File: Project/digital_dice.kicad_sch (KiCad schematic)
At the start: 26 parts, among them SW1 SW_Push, U1 74LS04, U2 74LS93, U3 74LS08, U4 74LS32

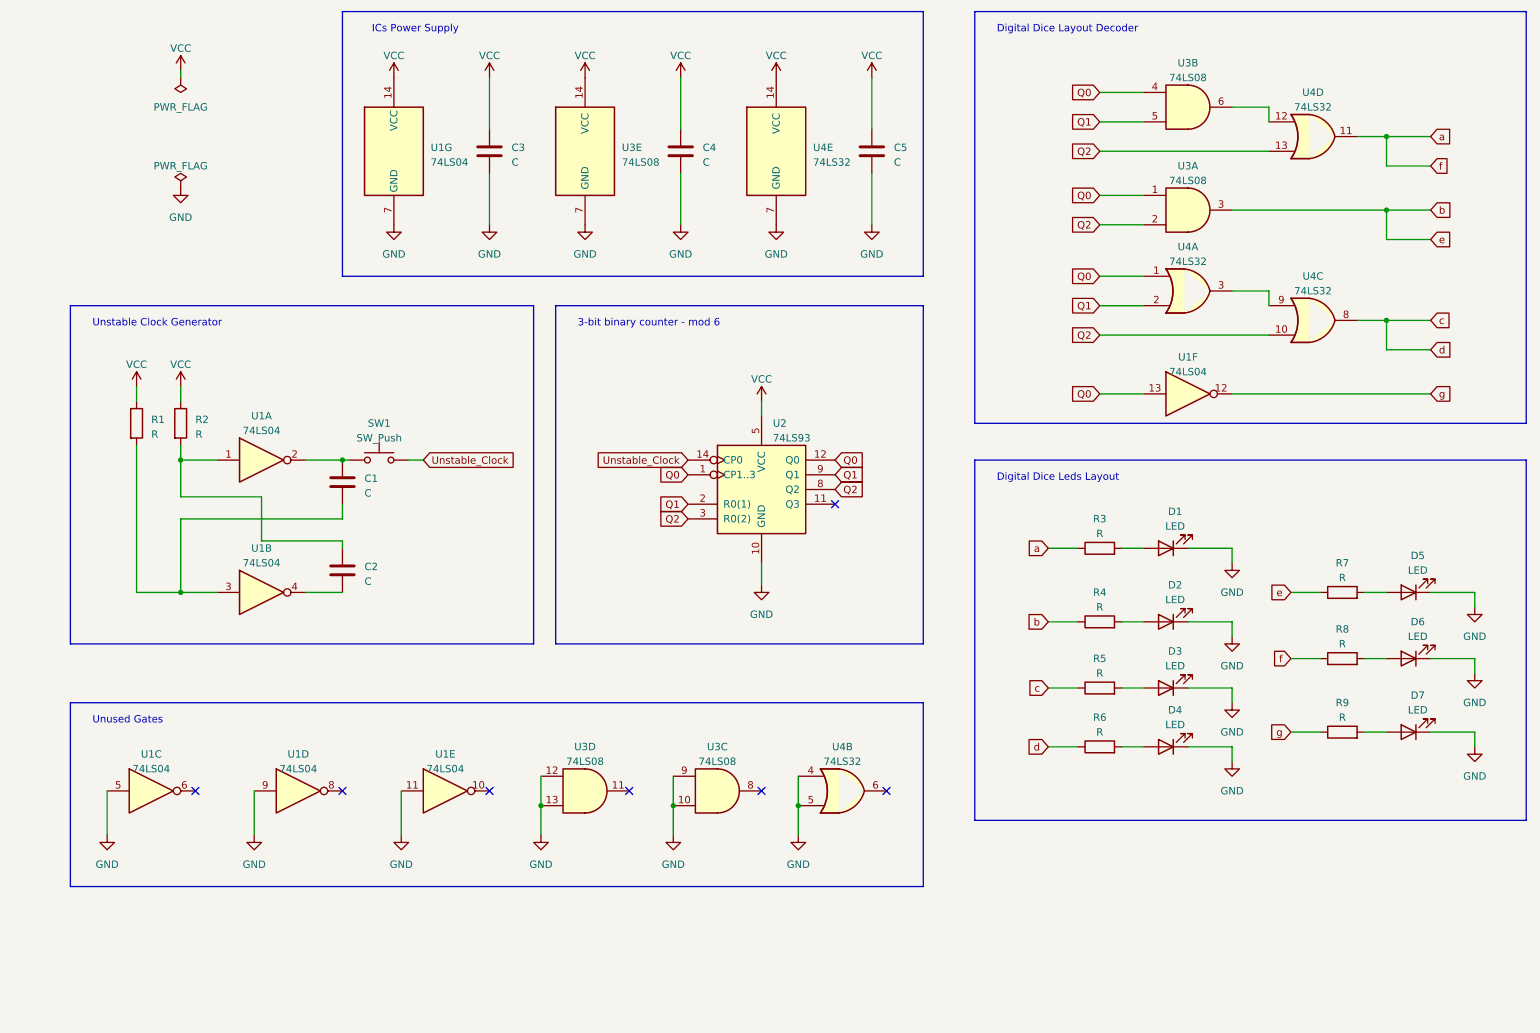
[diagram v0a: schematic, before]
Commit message: assigned components values and footprints
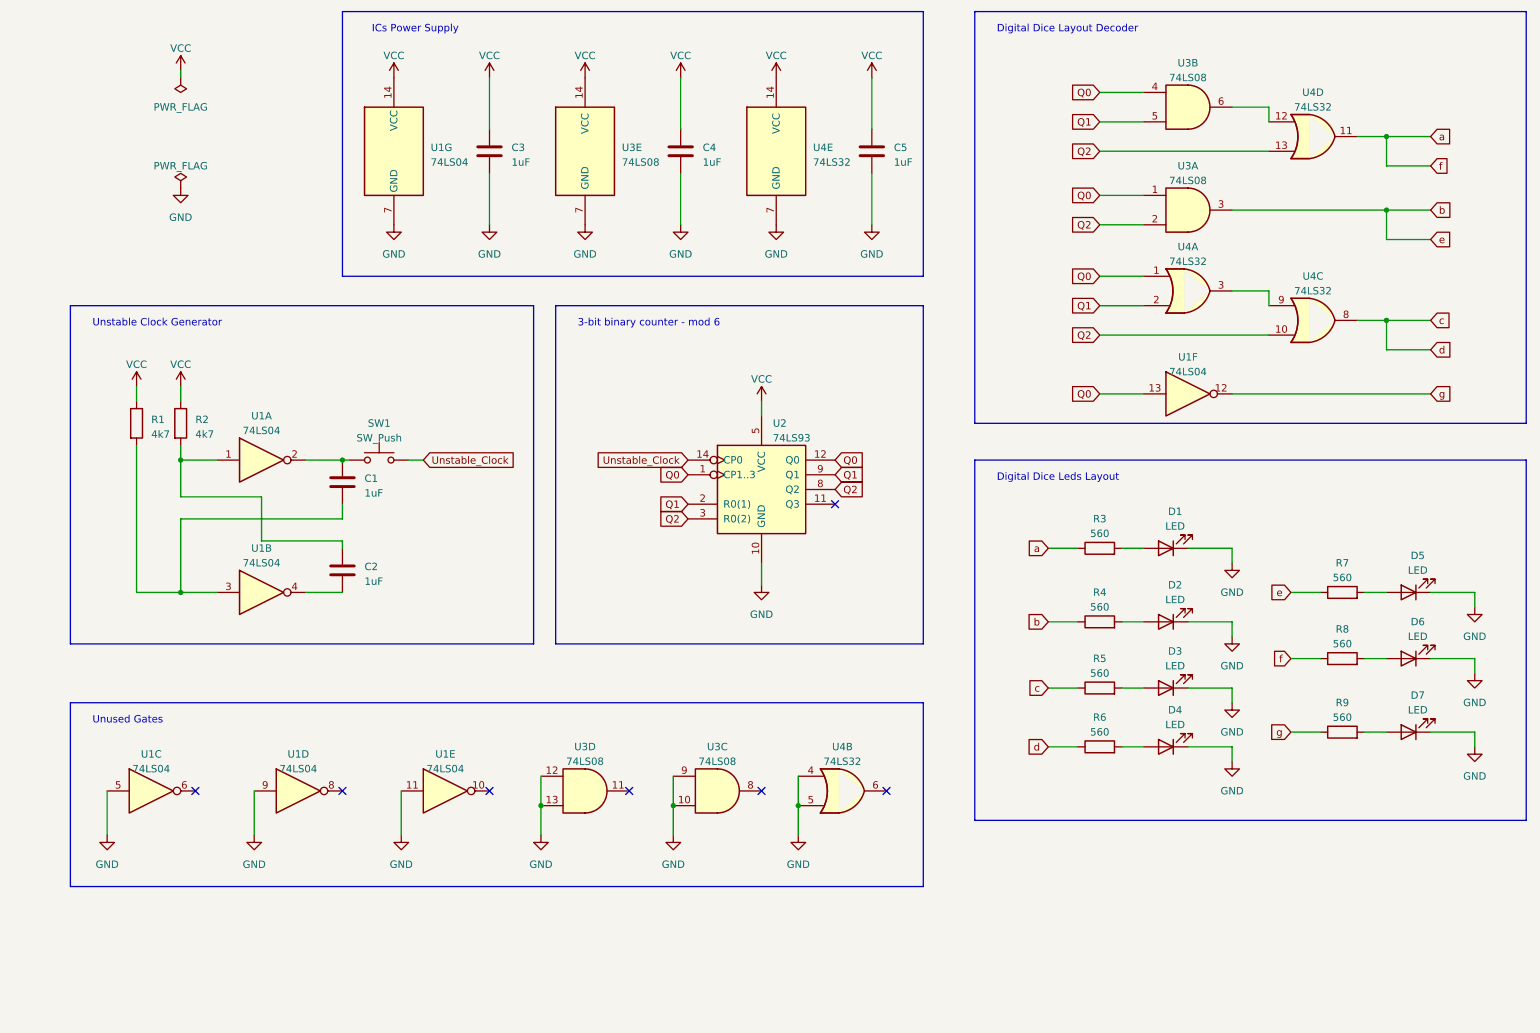
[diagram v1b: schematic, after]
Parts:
- C1, C2, C3, C4, C5: value C -> 1uF; footprint (none) -> Capacitor_THT:CP_Radial_D5.0mm_P2.50mm
- D1, D2, D3, D4, D5, D6, D7: footprint (none) -> LED_THT:LED_D5.0mm
- R1, R2: value R -> 4k7; footprint (none) -> Resistor_THT:R_Axial_DIN0207_L6.3mm_D2.5mm_P7.62mm_Horizontal
- R3, R4, R5, R6, R7, R8, R9: value R -> 560; footprint (none) -> Resistor_THT:R_Axial_DIN0207_L6.3mm_D2.5mm_P7.62mm_Horizontal
- SW1: footprint (none) -> Button_Switch_THT:SW_PUSH_6mm
- U1, U2, U3, U4: footprint (none) -> Package_DIP:DIP-14_W7.62mm

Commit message: changed leds and button to pin headers, added main power supply
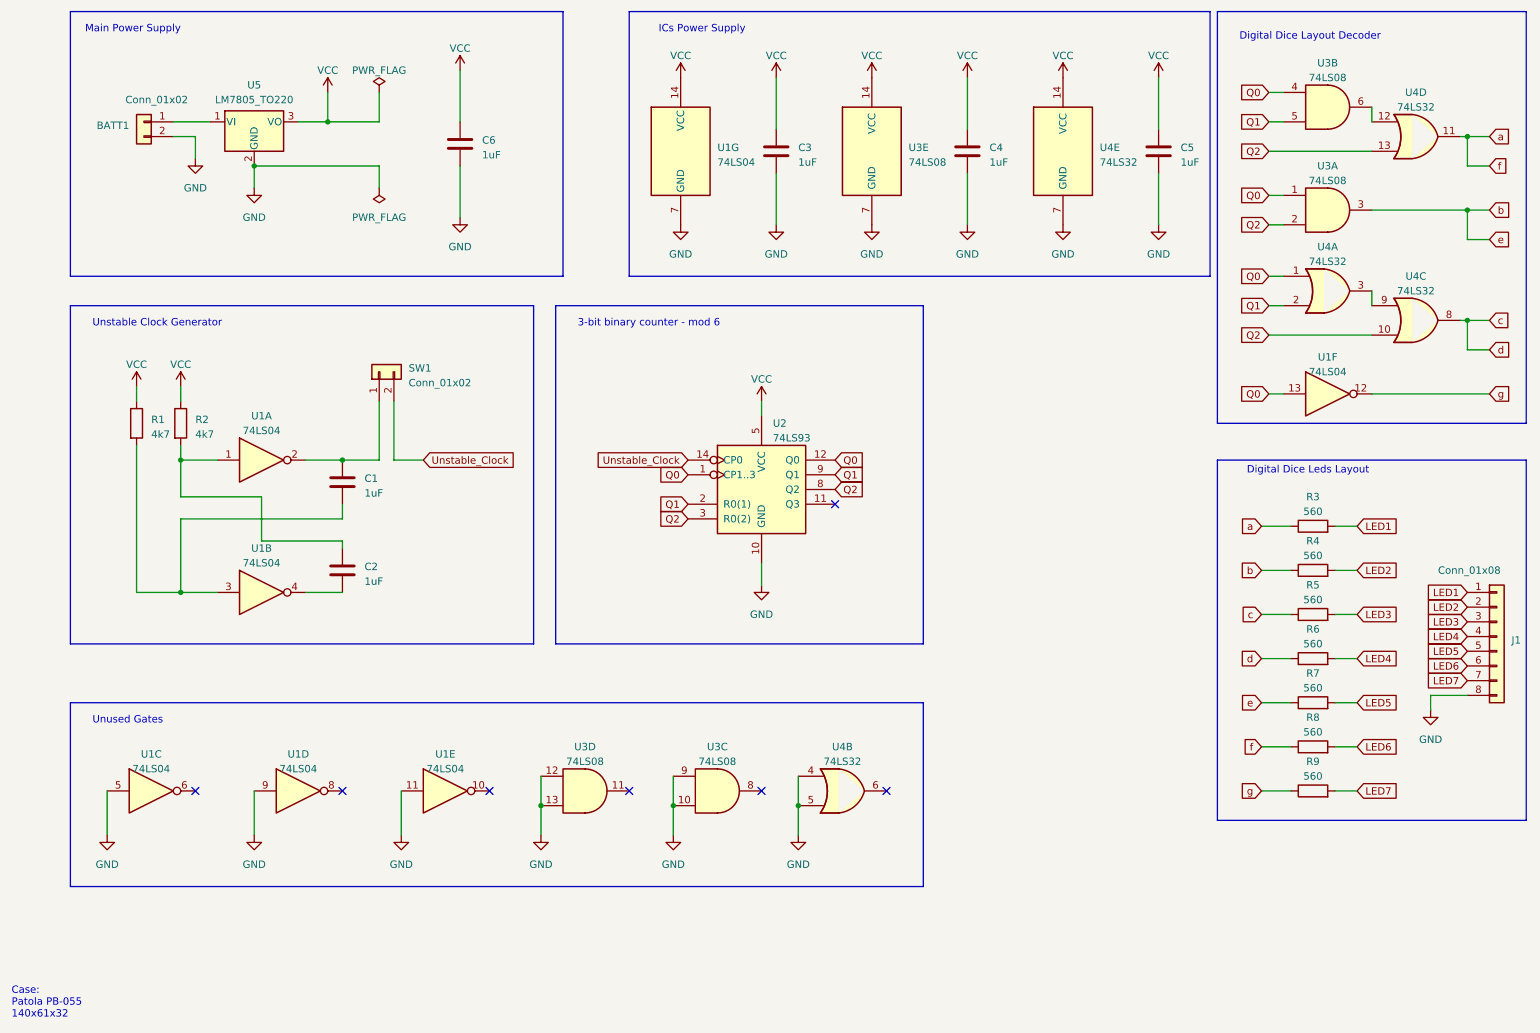
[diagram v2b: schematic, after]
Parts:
- removed D1, D2, D3, D4, D5, D6, D7: LED, LED_THT:LED_D5.0mm, symbol Device:LED
- removed SW1: SW_Push, Button_Switch_THT:SW_PUSH_6mm, symbol Switch:SW_Push
- added BATT1, SW1: Conn_01x02, Connector_PinHeader_2.54mm:PinHeader_1x02_P2.54mm_Vertical, symbol Connector_Generic:Conn_01x02
- added C6: 1uF, Capacitor_THT:CP_Radial_D5.0mm_P2.50mm, symbol Device:C
- added J1: Conn_01x08, Connector_PinHeader_2.54mm:PinHeader_1x08_P2.54mm_Vertical, symbol Connector_Generic:Conn_01x08
- added U5: LM7805_TO220, Package_TO_SOT_THT:TO-220-3_Vertical, symbol Regulator_Linear:LM7805_TO220
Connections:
- net GND: now also BATT1.2 (Pin_2), C6.2, J1.8 (Pin_8), U5.2 (GND)
- net Unstable_Clock: now also SW1.2 (Pin_2)
- net VCC: now also C6.1, U5.3 (VO)
- net LED3: now reaches R5.2
- net LED3: now also J1.3 (Pin_3)
- net LED2: now reaches R4.2
- net LED2: now also J1.2 (Pin_2)
- net LED6: now reaches R8.2
- net LED6: now also J1.6 (Pin_6)
- net LED1: now reaches R3.2
- net LED1: now also J1.1 (Pin_1)
- net at C1.1, U1.2: now also SW1.1 (Pin_1)
- net LED7: now reaches R9.2
- net LED7: now also J1.7 (Pin_7)
- net LED4: now reaches R6.2
- net LED4: now also J1.4 (Pin_4)
- net LED5: now reaches R7.2
- net LED5: now also J1.5 (Pin_5)
- new net: BATT1.1 (Pin_1), U5.1 (VI)
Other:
- note added: "Case: Patola PB-055 140x61x32"
- note added: "Main Power Supply"
- moved on the sheet: C3, C4, C5, R3, R4, R5, R6, R7, R8, R9, U1F, U1G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

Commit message: separated project in sheets
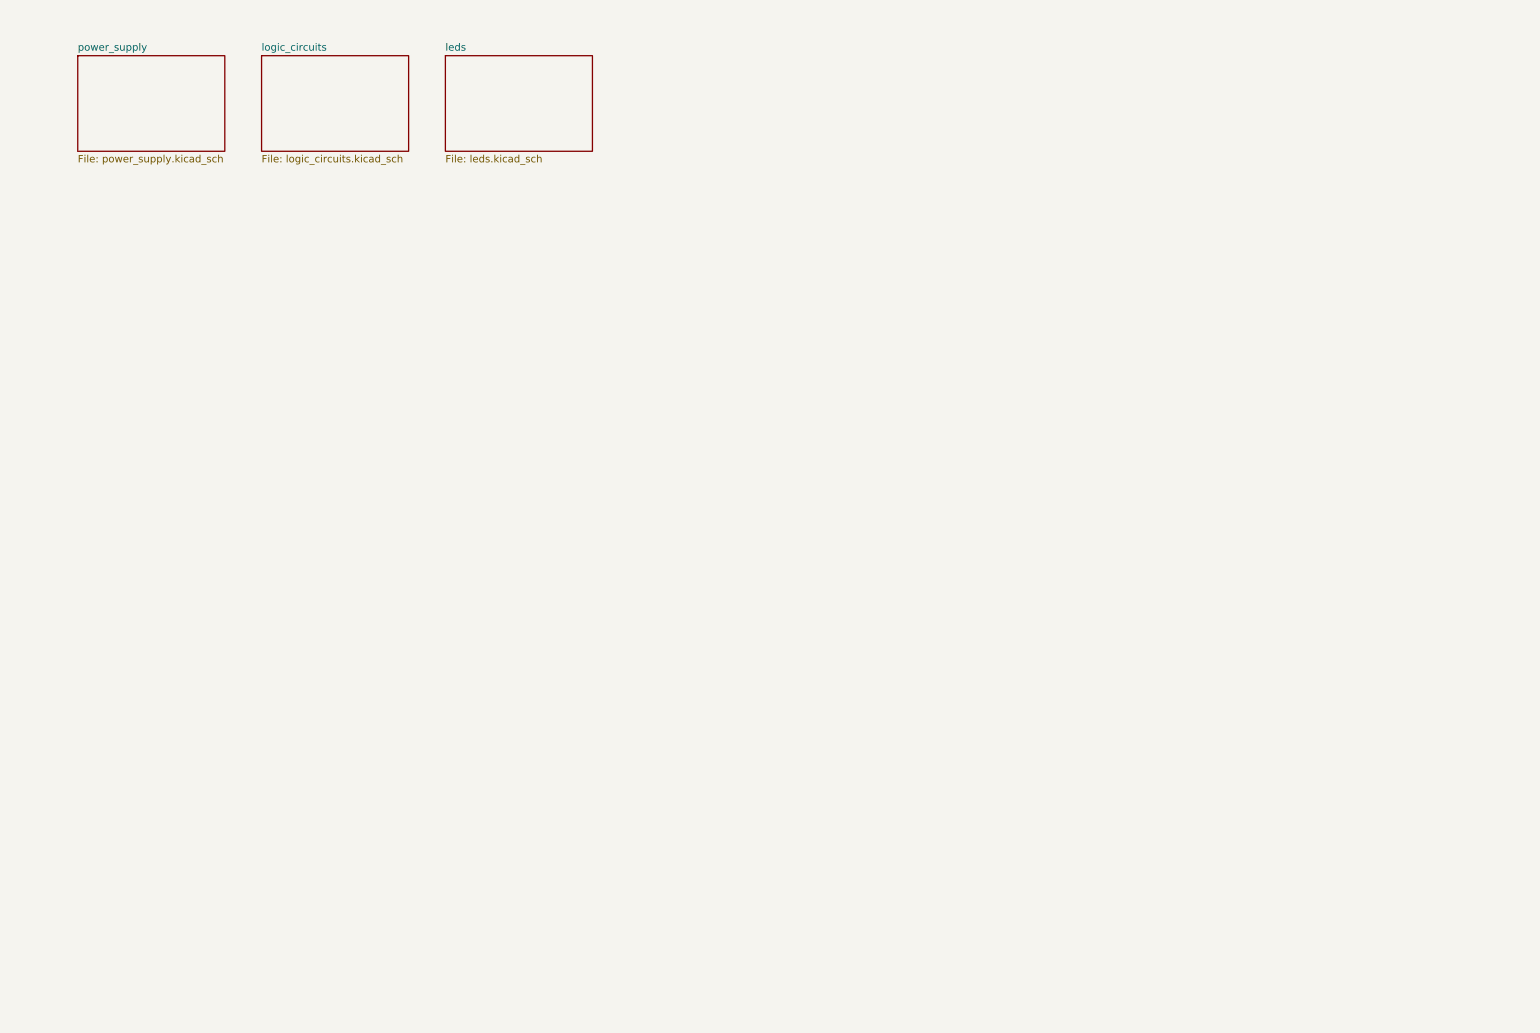
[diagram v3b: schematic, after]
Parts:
- removed BATT1, SW1: Conn_01x02, Connector_PinHeader_2.54mm:PinHeader_1x02_P2.54mm_Vertical, symbol Connector_Generic:Conn_01x02
- removed C1, C2, C3, C4, C5, C6: 1uF, Capacitor_THT:CP_Radial_D5.0mm_P2.50mm, symbol Device:C
- removed J1: Conn_01x08, Connector_PinHeader_2.54mm:PinHeader_1x08_P2.54mm_Vertical, symbol Connector_Generic:Conn_01x08
- removed R1, R2: 4k7, Resistor_THT:R_Axial_DIN0207_L6.3mm_D2.5mm_P7.62mm_Horizontal, symbol Device:R
- removed R3, R4, R5, R6, R7, R8, R9: 560, Resistor_THT:R_Axial_DIN0207_L6.3mm_D2.5mm_P7.62mm_Horizontal, symbol Device:R
- removed U1: 74LS04, Package_DIP:DIP-14_W7.62mm, symbol 74xx:74LS04
- removed U2: 74LS93, Package_DIP:DIP-14_W7.62mm, symbol 74xx:74LS93
- removed U3: 74LS08, Package_DIP:DIP-14_W7.62mm, symbol 74xx:74LS08
- removed U4: 74LS32, Package_DIP:DIP-14_W7.62mm, symbol 74xx:74LS32
- removed U5: LM7805_TO220, Package_TO_SOT_THT:TO-220-3_Vertical, symbol Regulator_Linear:LM7805_TO220
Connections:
- no-connect marks 7 -> 0
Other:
- added sheet leds (leds.kicad_sch)
- added sheet logic_circuits (logic_circuits.kicad_sch)
- added sheet power_supply (power_supply.kicad_sch)
- note removed: "3-bit binary counter - mod 6"
- note removed: "Case: Patola PB-055 140x61x32"
- note removed: "Digital Dice Layout Decoder"
- note removed: "Digital Dice Leds Layout"
- note removed: "ICs Power Supply"
- note removed: "Main Power Supply"
- note removed: "Unstable Clock Generator"
- note removed: "Unused Gates"

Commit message: routing complete
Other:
- removed sheet leds
- company: (none) -> Marcos Yonamine
- title: (none) -> Digital Dice
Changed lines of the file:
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@@
-(kicad_sch (version 20230121) (generator eeschema)
-  (paper "A4")
-  (sheet (at 91.44 26.67) (size 25.4 16.51) (fields_autoplaced)
-    (stroke (width 0.1524) (type solid))
-    (fill (color 0 0 0 0.0000))
-    (property "Sheetname" "leds" (at 91.44 25.9584 0)
-      (effects (font (size 1.27 1.27)) (justify left bottom))
-    )
-    (property "Sheetfile" "leds.kicad_sch" (at 91.44 43.7646 0)
-      (effects (font (size 1.27 1.27)) (justify left top))
-    )
-    (instances
-      (project "digital_dice"
-        (path "/3fd45f8c-51ef-4454-9e54-21b96824f914" (page "4"))
-      )
-    )
-  )
-  (sheet (at 27.94 26.67) (size 25.4 16.51) (fields_autoplaced)
-    (stroke (width 0.1524) (type solid))
-    (fill (color 0 0 0 0.0000))
-    (property "Sheetname" "power_supply" (at 27.94 25.9584 0)
-      (effects (font (size 1.27 1.27)) (justify left bottom))
-    )
-    (property "Sheetfile" "power_supply.kicad_sch" (at 27.94 43.7646 0)
-      (effects (font (size 1.27 1.27)) (justify left top))
-    )
-    (instances
-      (project "digital_dice"
-        (path "/3fd45f8c-51ef-4454-9e54-21b96824f914" (page "2"))
-      )
-    )
-  )
-  (sheet (at 59.69 26.67) (size 25.4 16.51) (fields_autoplaced)
-    (stroke (width 0.1524) (type solid))
-    (fill (color 0 0 0 0.0000))
-    (property "Sheetname" "logic_circuits" (at 59.69 25.9584 0)
-      (effects (font (size 1.27 1.27)) (justify left bottom))
-    )
-    (property "Sheetfile" "logic_circuits.kicad_sch" (at 59.69 43.7646 0)
-      (effects (font (size 1.27 1.27)) (justify left top))
-    )
-    (instances
-      (project "digital_dice"
-        (path "/3fd45f8c-51ef-4454-9e54-21b96824f914" (page "3"))
-      )
-    )
-  )
-  (sheet_instances
-    (path "/" (page "1"))
-  )
+(kicad_sch
+	(version 20231120)
+	(generator "eeschema")
+	(generator_version "8.0")
+	(paper "A4")
+	(title_block
+		(title "Digital Dice")
+		(date "2024-10-06")
+		(company "Marcos Yonamine")
+	)
+	(sheet
+		(at 27.94 26.67)
+		(size 25.4 16.51)
+		(fields_autoplaced yes)
+		(stroke
+			(width 0.1524)
+			(type solid)
+		)
+		(fill
+			(color 0 0 0 0.0000)
+		)
+		(property "Sheetname" "power_supply"
+			(at 27.94 25.9584 0)
+			(effects
+				(font
+					(size 1.27 1.27)
+				)
+				(justify left bottom)
+			)
+		)
+		(property "Sheetfile" "power_supply.kicad_sch"
+			(at 27.94 43.7646 0)
+			(effects
+				(font
+					(size 1.27 1.27)
+				)
+				(justify left top)
+			)
+		)
+		(instances
+			(project "digital_dice"
+				(path "/3fd45f8c-51ef-4454-9e54-21b96824f914"
+					(page "2")
+				)
+			)
+		)
+	)
+	(sheet
+		(at 59.69 26.67)
+		(size 25.4 16.51)
+		(fields_autoplaced yes)
+		(stroke
+			(width 0.1524)
+			(type solid)
+		)
+		(fill
+			(color 0 0 0 0.0000)
+		)
+		(property "Sheetname" "logic_circuits"
+			(at 59.69 25.9584 0)
+			(effects
+				(font
+					(size 1.27 1.27)
+				)
+				(justify left bottom)
+			)
+		)
+		(property "Sheetfile" "logic_circuits.kicad_sch"
+			(at 59.69 43.7646 0)
+			(effects
+				(font
+					(size 1.27 1.27)
+				)
+				(justify left top)
+			)
+		)
+		(instances
+			(project "digital_dice"
+				(path "/3fd45f8c-51ef-4454-9e54-21b96824f914"
+					(page "3")
+				)
+			)
+		)
+	)
+	(sheet_instances
+		(path "/"
+			(page "1")
+		)
+	)
 )
